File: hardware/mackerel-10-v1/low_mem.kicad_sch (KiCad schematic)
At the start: 4 parts, among them U2 AS6C4008-55PCN, U3 SST39SF040, U4 AS6C4008-55PCN, U5 SST39SF040

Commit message: Trying to figure out Mackerel-10 components
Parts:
- removed U2, U4: AS6C4008-55PCN, Package_DIP:DIP-32_W15.24mm, symbol Memory_RAM:AS6C4008-55PCN
- added U4, U6: KM62256CLP, Package_DIP:DIP-28_W15.24mm, symbol Memory_RAM:KM62256CLP
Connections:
- net +5V: now also U4.28 (VCC), U6.28 (VCC)
- net A1: now also U4.10 (A0), U6.10 (A0)
- net A10: now also U4.24 (A9), U6.24 (A9)
- net A11: now also U4.21 (A10), U6.21 (A10)
- net A12: now also U4.23 (A11), U6.23 (A11)
- net A13: now also U4.2 (A12), U6.2 (A12)
- net A14: now also U4.26 (A13), U6.26 (A13)
- net A15: now also U4.1 (A14), U6.1 (A14)
- net A2: now also U4.9 (A1), U6.9 (A1)
- net A3: now also U4.8 (A2), U6.8 (A2)
- net A4: now also U4.7 (A3), U6.7 (A3)
- net A5: now also U4.6 (A4), U6.6 (A4)
- net A6: now also U4.5 (A5), U6.5 (A5)
- net A7: now also U4.4 (A6), U6.4 (A6)
- net A8: now also U4.3 (A7), U6.3 (A7)
- net A9: now also U4.25 (A8), U6.25 (A8)
- net D0: now also U6.11 (Q0)
- net D1: now also U6.12 (Q1)
- net D10: now also U4.13 (Q2)
- net D11: now also U4.15 (Q3)
- net D12: now also U4.16 (Q4)
- net D13: now also U4.17 (Q5)
- net D14: now also U4.18 (Q6)
- net D15: now also U4.19 (Q7)
- net D2: now also U6.13 (Q2)
- net D3: now also U6.15 (Q3)
- net D4: now also U6.16 (Q4)
- net D5: now also U6.17 (Q5)
- net D6: now also U6.18 (Q6)
- net D7: now also U6.19 (Q7)
- net D8: now also U4.11 (Q0)
- net D9: now also U4.12 (Q1)
- net GND: now also U4.14 (GND), U6.14 (GND)

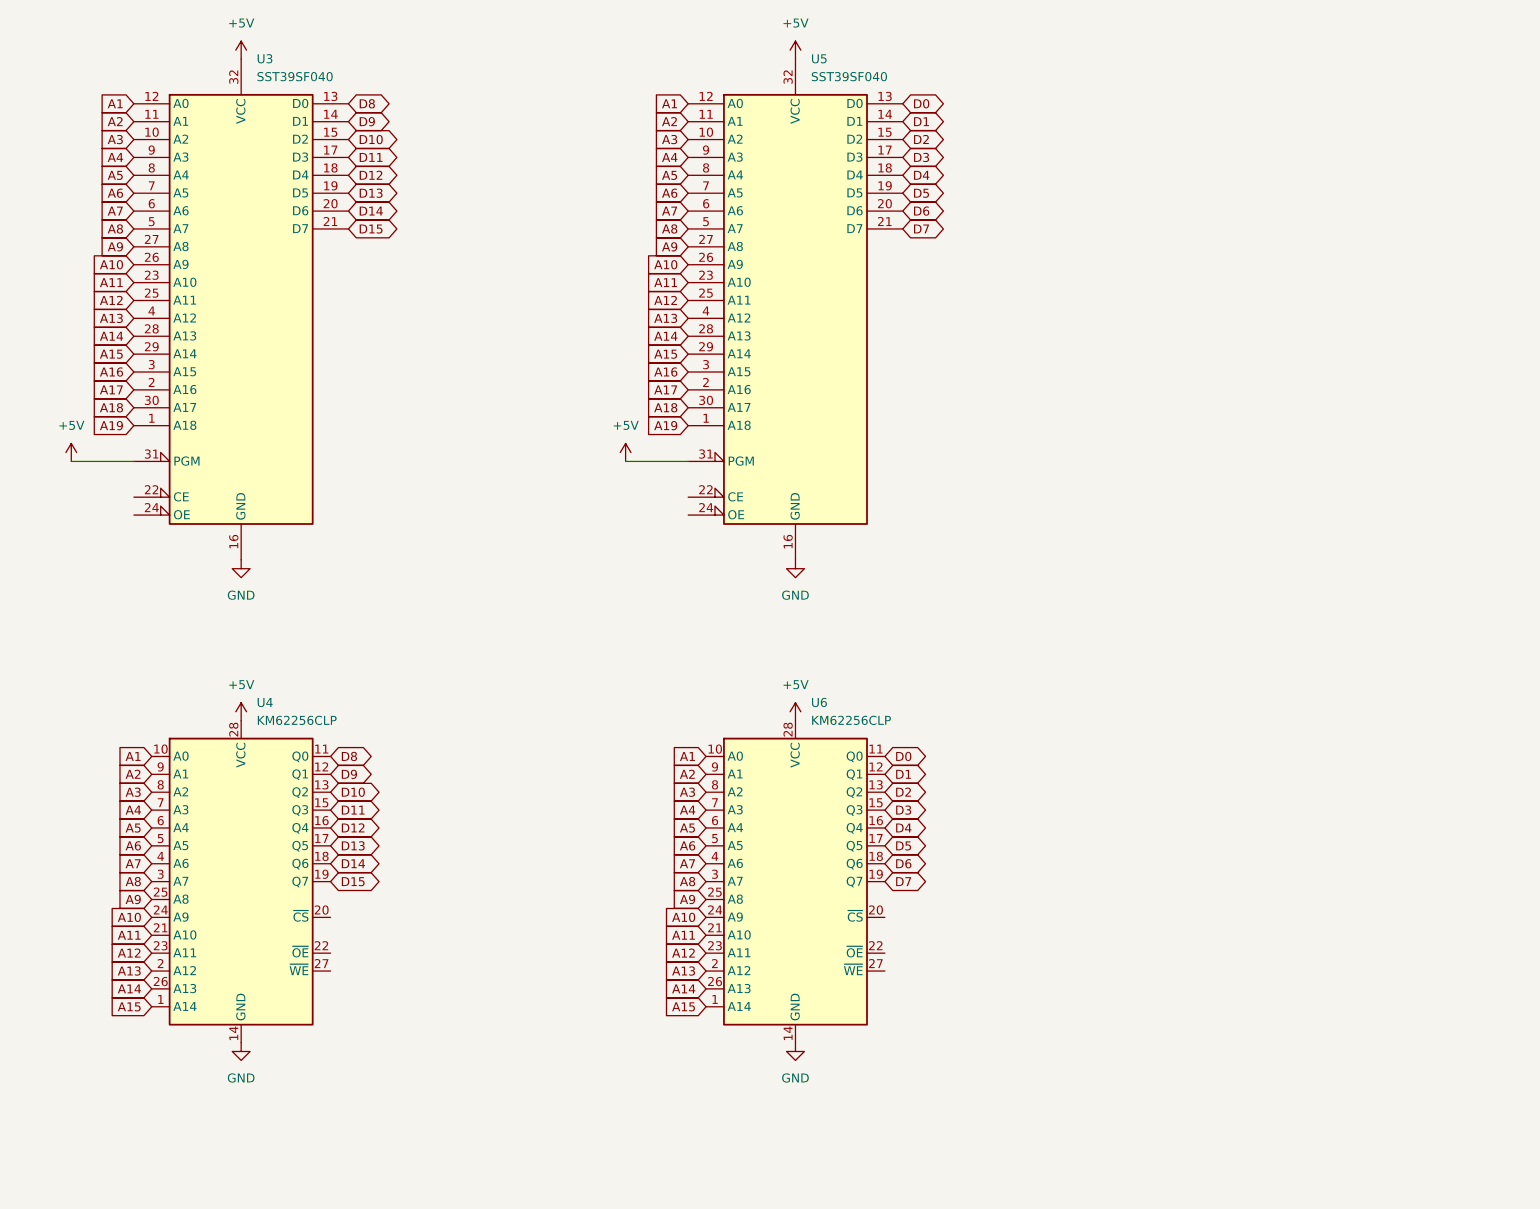
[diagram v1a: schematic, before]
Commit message: More progress on Mackerel-10 schematic and PCB
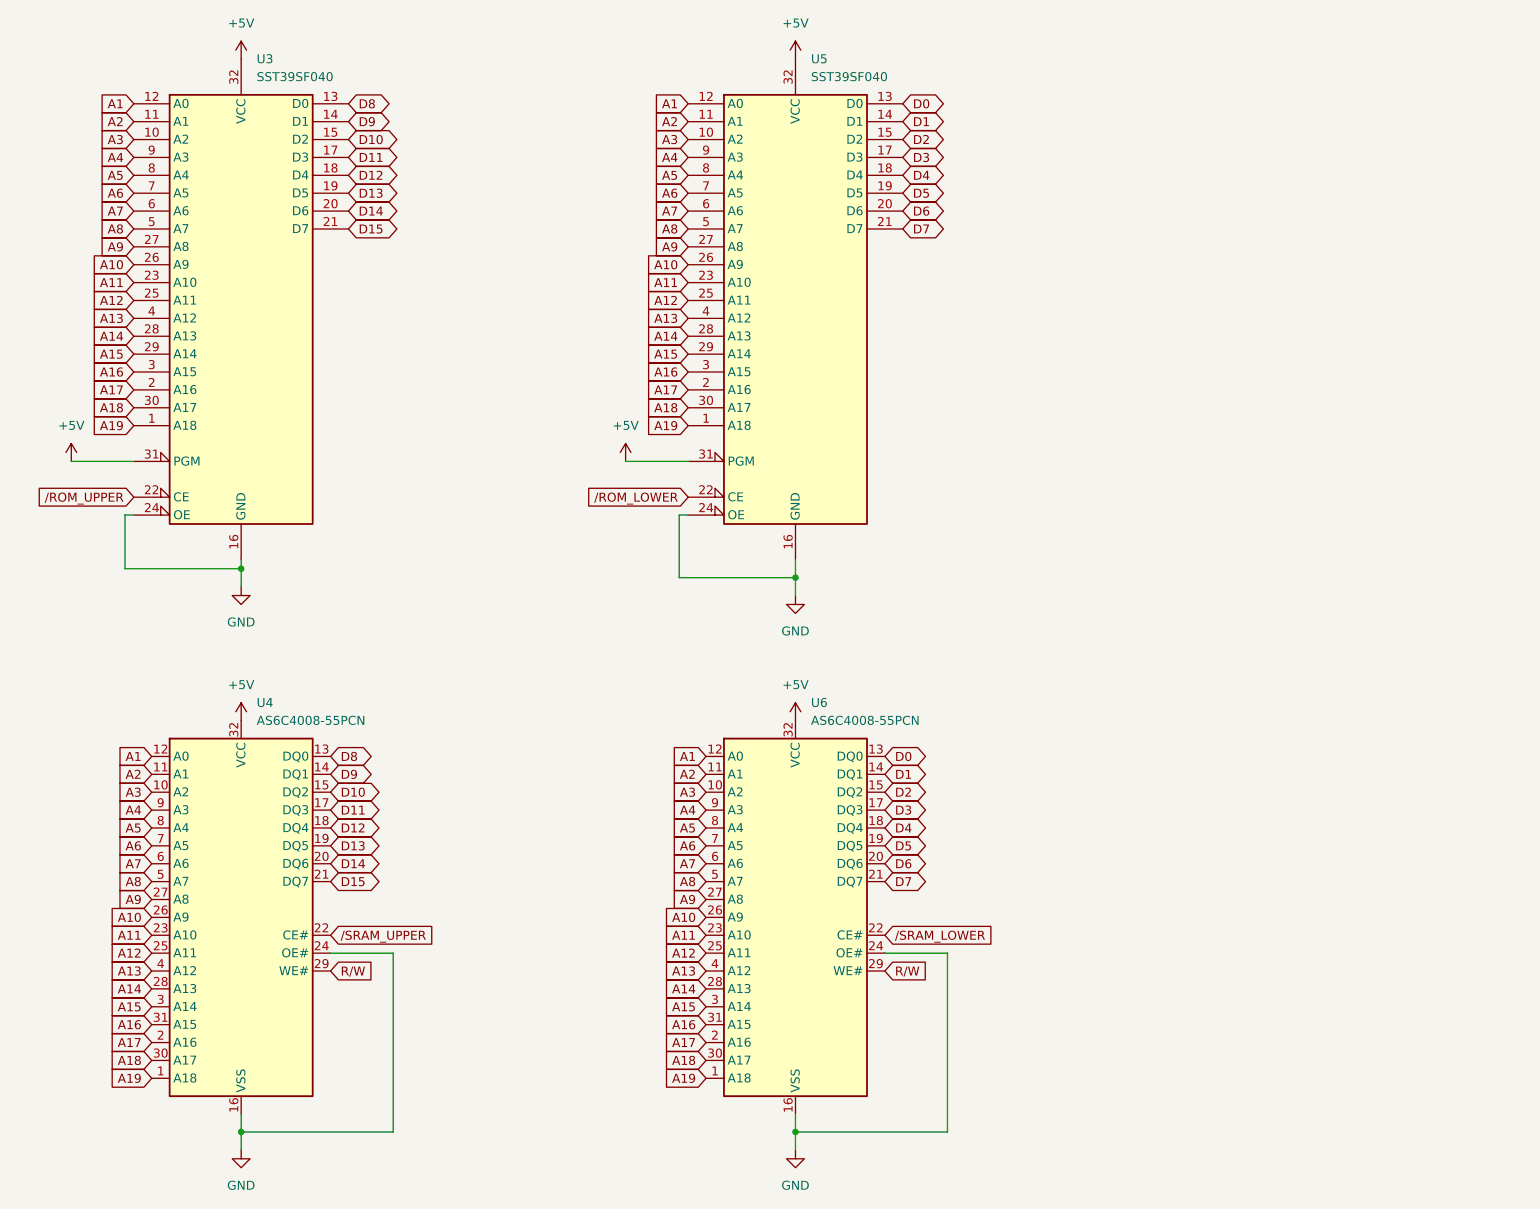
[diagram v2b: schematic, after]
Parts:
- removed U4, U6: KM62256CLP, Package_DIP:DIP-28_W15.24mm, symbol Memory_RAM:KM62256CLP
- added U4, U6: AS6C4008-55PCN, Package_DIP:DIP-32_W15.24mm, symbol Memory_RAM:AS6C4008-55PCN
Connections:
- net +5V: now also U4.32 (VCC), U6.32 (VCC)
- net A1: now also U4.12 (A0), U6.12 (A0)
- net A10: now also U4.26 (A9), U6.26 (A9)
- net A11: now also U4.23 (A10), U6.23 (A10)
- net A12: now also U4.25 (A11), U6.25 (A11)
- net A13: now also U4.4 (A12), U6.4 (A12)
- net A14: now also U4.28 (A13), U6.28 (A13)
- net A15: now also U4.3 (A14), U6.3 (A14)
- net A16: now also U4.31 (A15), U6.31 (A15)
- net A17: now also U4.2 (A16), U6.2 (A16)
- net A18: now also U4.30 (A17), U6.30 (A17)
- net A19: now also U4.1 (A18), U6.1 (A18)
- net A2: now also U4.11 (A1), U6.11 (A1)
- net A3: now also U4.10 (A2), U6.10 (A2)
- net A4: now also U4.9 (A3), U6.9 (A3)
- net A5: now also U4.8 (A4), U6.8 (A4)
- net A6: now also U4.7 (A5), U6.7 (A5)
- net A7: now also U4.6 (A6), U6.6 (A6)
- net A8: now also U4.5 (A7), U6.5 (A7)
- net A9: now also U4.27 (A8), U6.27 (A8)
- net D0: now also U6.13 (DQ0)
- net D1: now also U6.14 (DQ1)
- net D10: now also U4.15 (DQ2)
- net D11: now also U4.17 (DQ3)
- net D12: now also U4.18 (DQ4)
- net D13: now also U4.19 (DQ5)
- net D14: now also U4.20 (DQ6)
- net D15: now also U4.21 (DQ7)
- net D2: now also U6.15 (DQ2)
- net D3: now also U6.17 (DQ3)
- net D4: now also U6.18 (DQ4)
- net D5: now also U6.19 (DQ5)
- net D6: now also U6.20 (DQ6)
- net D7: now also U6.21 (DQ7)
- net D8: now also U4.13 (DQ0)
- net D9: now also U4.14 (DQ1)
- net GND: now also U3.24 (OE), U5.24 (OE), U4.16 (VSS), U4.24 (OE#), U6.16 (VSS), U6.24 (OE#)
- net /ROM_UPPER: now reaches U3.22 (CE)
- net /ROM_LOWER: now reaches U5.22 (CE)
- new net R/W: U4.29 (WE#), U6.29 (WE#)
- new net /SRAM_LOWER: U6.22 (CE#)
- new net /SRAM_UPPER: U4.22 (CE#)

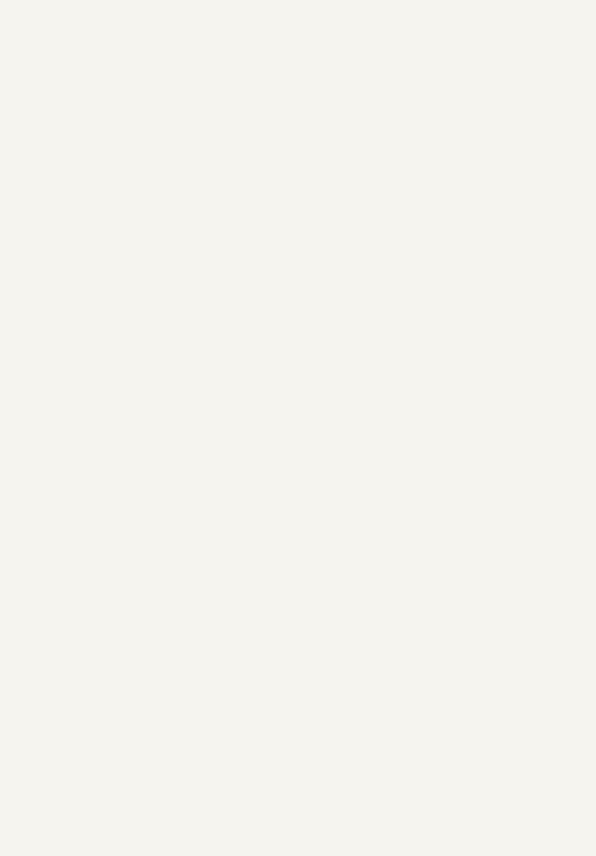
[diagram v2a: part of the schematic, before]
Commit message: Mack-10 proto routed except for expansion headers
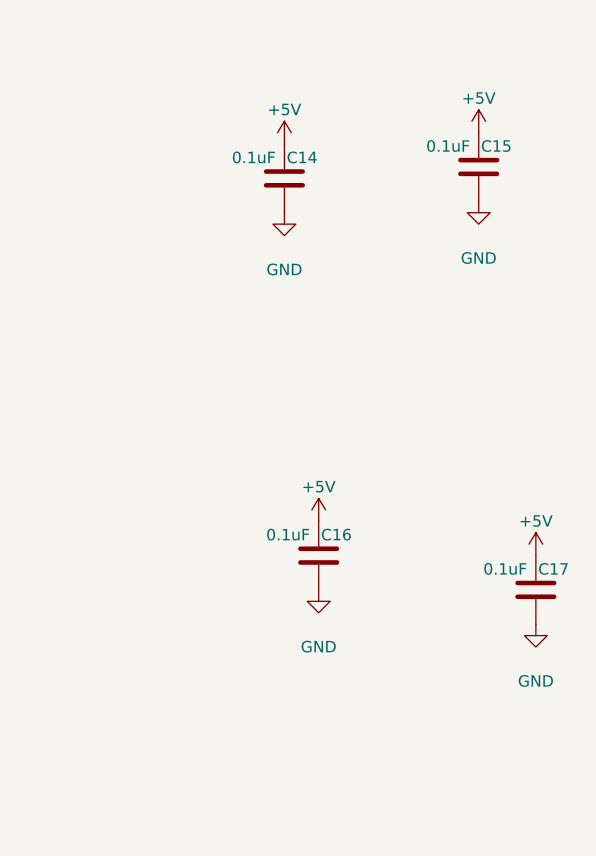
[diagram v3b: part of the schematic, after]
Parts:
- added C14, C15, C16, C17: 0.1uF, Capacitor_THT:C_Disc_D4.7mm_W2.5mm_P5.00mm, symbol Device:C
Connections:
- net +5V: now also C14.1, C15.1, C16.1, C17.1
- net GND: now also C14.2, C15.2, C16.2, C17.2

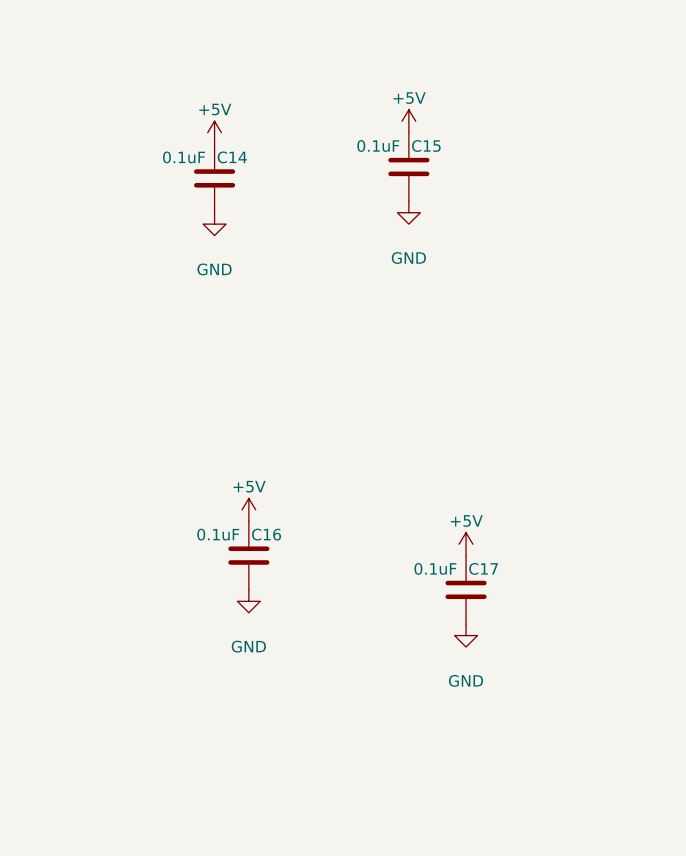
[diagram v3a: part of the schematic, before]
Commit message: Mackerel-10 proto board ready for manufacturing
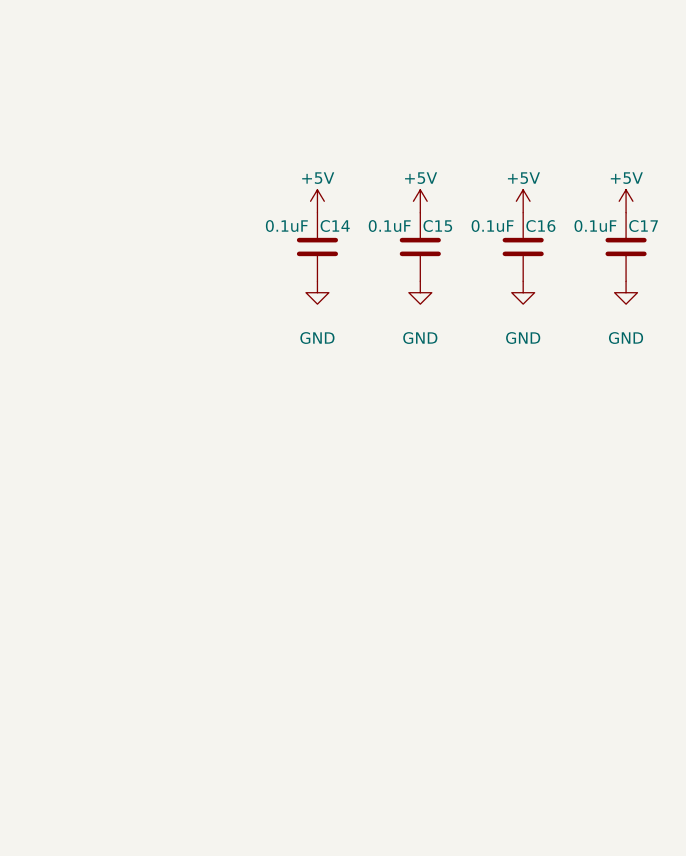
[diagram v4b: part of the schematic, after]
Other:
- moved on the sheet: C14, C15, C16, C17
